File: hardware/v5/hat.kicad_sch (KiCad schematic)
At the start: 6 parts, among them J1 GPIO, U1 CAT24C256

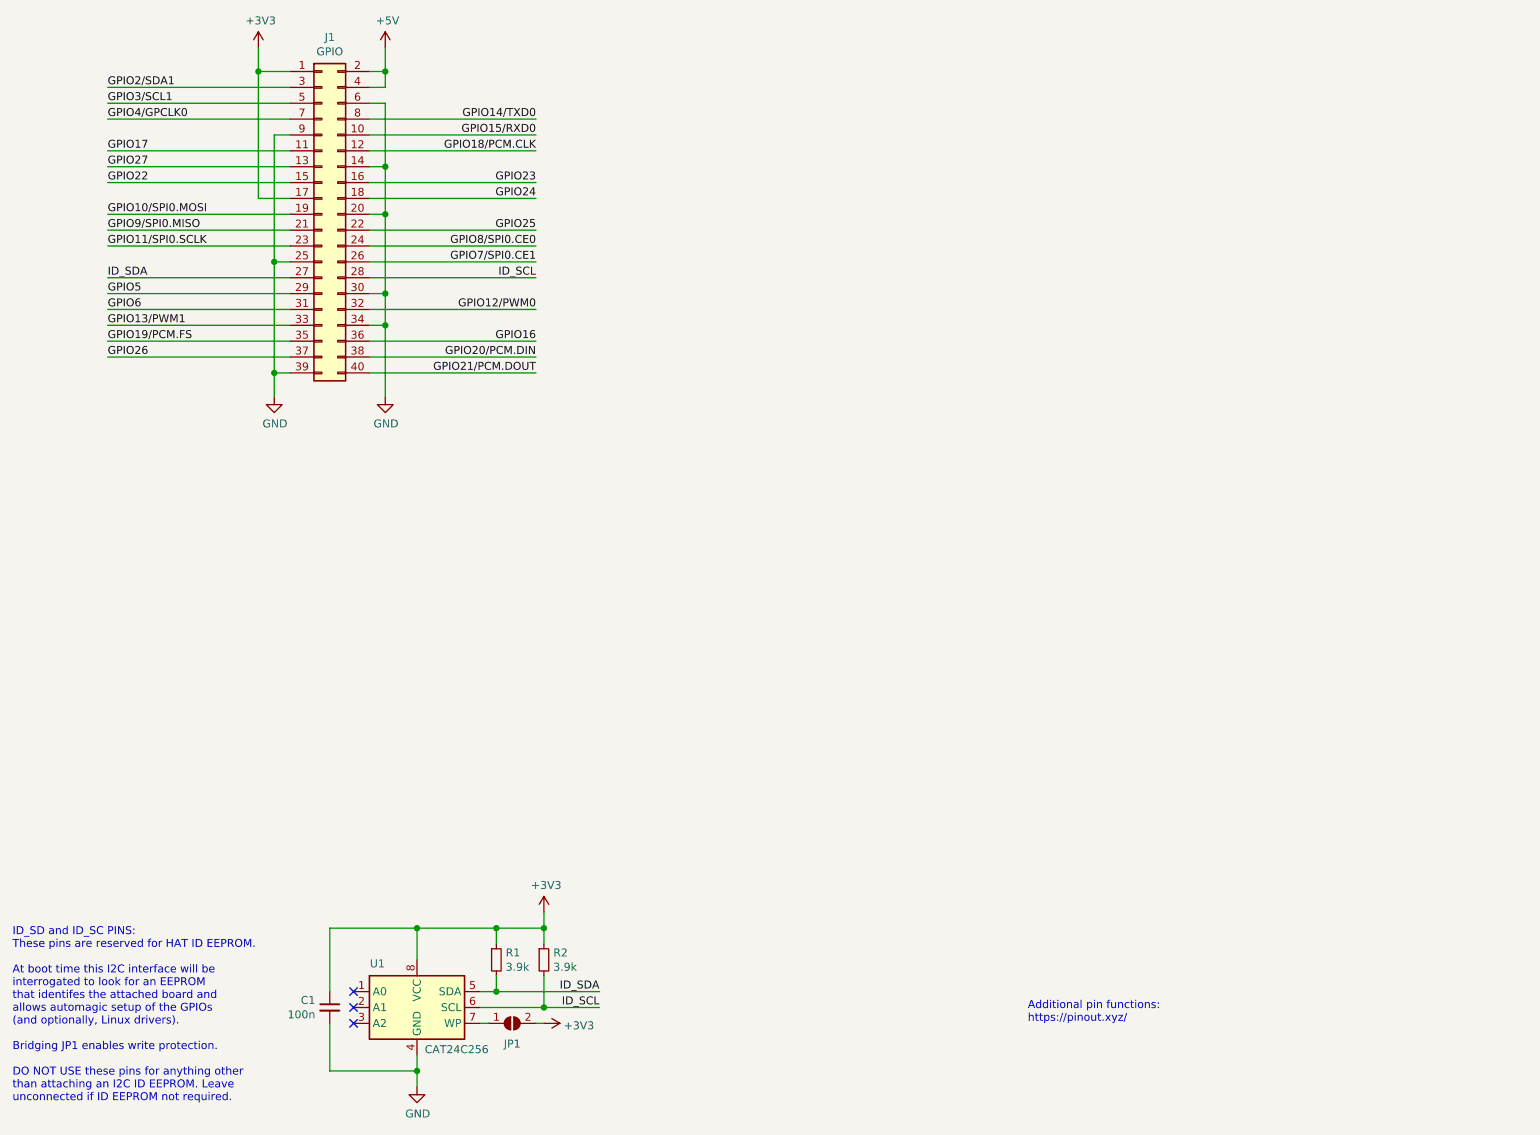
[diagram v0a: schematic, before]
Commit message: v5: import/reimplement parport design on template
Problem: template board is still blank.

Adjust board edge to handle SMT header and add cutout for pi5 camera/
display FFC connectors.  For GPIO connector, use existing kicad 8 Harwin
M20 series footprint but adjust the pinout for top of board pi GPIO,
and adjust position since centroid moved from THT pin 1 to SMT centroid.
Add keepout for pi5 PoE like the existing one for pi4.

Import the SN74LVC16128 symbol from the v4 board.  Orient the chip
as before for best routing but aim for tighter traces this time.
Add bypass caps to all power inputs for good measure.  Chip capacitors
and resistors are shrunk from 0805 to 0603 in this revision.  Allow the
cable VCC to be jumpered to either 5V or 3V3 per the spec sheet.

Move the EEPROM to the east end of the board for more direct routing.
Add a strong 1K pull-up to the template's WP jumper per the HAT+ spec.
Orient the chip the same direction as the SN74LVC16128 to avoid confusion.

Add the DB-25 right-angle 2x13 header on the west end as before.
This time, use a custom header footprint so the DB-25 pin numbers can
be mirrored on the header.  Also, add a board cutout to improve insertion
ergonmics if the right angle header is used.

Implement the GPIO reassignments proposed in #67.  This should allow
I2C, UART0, and PWM0 to be used in stacked HATs.

Add a Sparkfun Qwiic connector to allow I2C expansion that way as well.
See: https://www.sparkfun.com/qwiic.

Put the official HAT+ logo on the board since this board complies with
https://datasheets.raspberrypi.com/hat/hat-plus-specification.pdf.
The logo image was provided via email along with marking guidelines.
Use the minimum 2.25mm height specified in the guidelines.

Add some helpful notes and the DB-25 pinout to the board silkscreen.
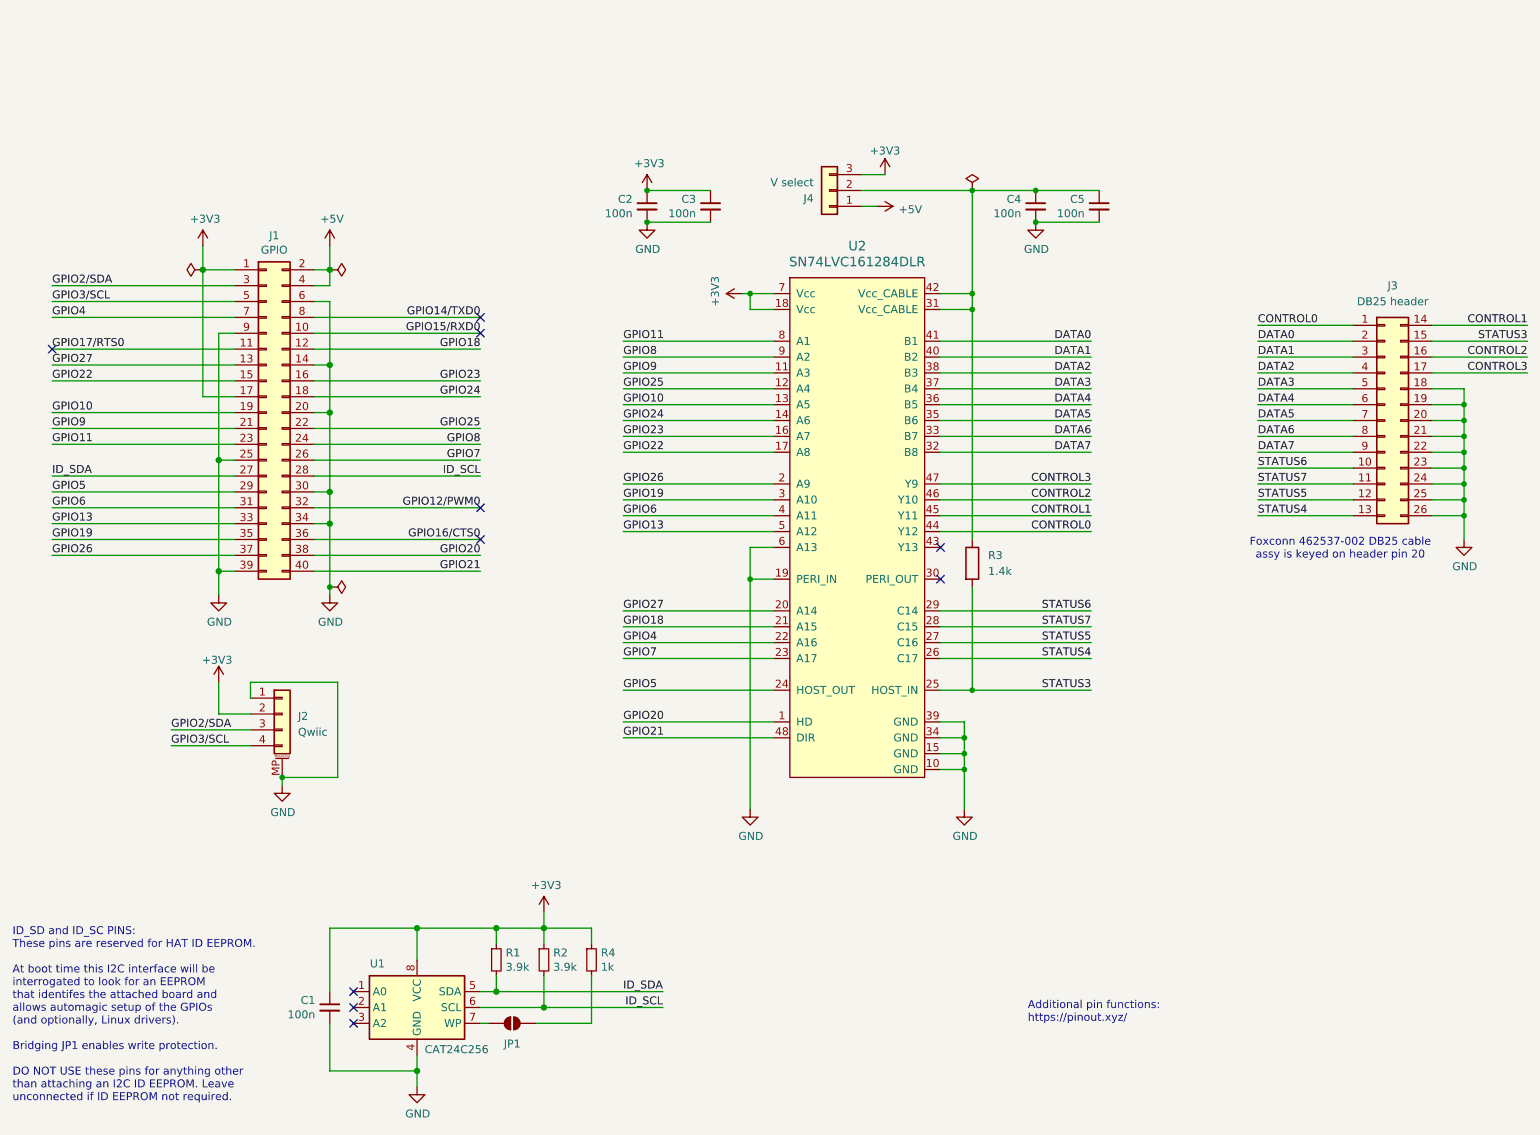
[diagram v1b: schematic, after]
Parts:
- added C2, C3, C4, C5: 100n, Capacitor_SMD:C_0603_1608Metric, symbol Device:C_Small
- added J2: Qwiic, Connector_JST:JST_SH_SM04B-SRSS-TB_1x04-1MP_P1.00mm_Horizontal, symbol Connector_Generic_MountingPin:Conn_01x04_MountingPin
- added J3: DB25 header, lib:DB25_header_2x13_P2.54mm_horizontal, symbol Connector_Generic:Conn_02x13_Top_Bottom
- added J4: V select, Connector_PinHeader_2.54mm:PinHeader_1x03_P2.54mm_Vertical, symbol Connector_Generic:Conn_01x03
- added R3: 1.4k, Resistor_SMD:R_0603_1608Metric, symbol Device:R
- added R4: 1k, Resistor_SMD:R_0603_1608Metric, symbol Device:R_Small
- added U2: SN74LVC161284DLR, Package_SO:SSOP-48_7.5x15.9mm_P0.635mm, symbol SN74LVC16128:SN74LVC161284DLR
- C1: footprint (none) -> Capacitor_SMD:C_0603_1608Metric
- J1: footprint Connector_PinSocket_2.54mm:PinSocket_2x20_P2.54mm_Vertical -> lib:Harwin_M20-7812045_2x20_P2.54mm_Vertical
- JP1: footprint (none) -> Jumper:SolderJumper-2_P1.3mm_Open_RoundedPad1.0x1.5mm
- R1, R2: footprint (none) -> Resistor_SMD:R_0603_1608Metric
- U1: footprint (none) -> Package_SO:SOIC-8_3.9x4.9mm_P1.27mm
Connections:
- net +3V3: now also C2.1, C3.1, J2.2 (Pin_2), J4.3 (Pin_3), R4.1, U2.18 (Vcc), U2.7 (Vcc); no longer JP1.2 (B)
- net +5V: now also J4.1 (Pin_1)
- net GND: now also C2.2, C3.2, C4.2, C5.2, J2.1 (Pin_1), J2.MP (MountPin), J3.18 (Pin_18), J3.19 (Pin_19), J3.20 (Pin_20), J3.21 (Pin_21), J3.22 (Pin_22), J3.23 (Pin_23), J3.24 (Pin_24), J3.25 (Pin_25), J3.26 (Pin_26), U2.10 (GND), U2.15 (GND), U2.19 (PERI_IN), U2.34 (GND), U2.39 (GND), U2.6 (A13)
- net GPIO22: now also U2.17 (A8)
- net GPIO23: now also U2.16 (A7)
- net GPIO24: now also U2.14 (A6)
- net GPIO25: now also U2.12 (A4)
- net GPIO26: now also U2.2 (A9)
- net GPIO27: now also U2.20 (A14)
- net GPIO5: now also U2.24 (HOST_OUT)
- net GPIO6: now also U2.4 (A11)
- net GPIO10/SPI0.MOSI renamed GPIO10
- net GPIO10: now also U2.13 (A5)
- net GPIO11/SPI0.SCLK renamed GPIO11
- net GPIO11: now also U2.8 (A1)
- net GPIO13/PWM1 renamed GPIO13
- net GPIO13: now also U2.5 (A12)
- net GPIO16 renamed GPIO16/CTS0
- net GPIO17 renamed GPIO17/RTS0
- net GPIO18/PCM.CLK renamed GPIO18
- net GPIO18: now also U2.21 (A15)
- net GPIO19/PCM.FS renamed GPIO19
- net GPIO19: now also U2.3 (A10)
- net GPIO20/PCM.DIN renamed GPIO20
- net GPIO20: now also U2.1 (HD)
- net GPIO21/PCM.DOUT renamed GPIO21
- net GPIO21: now also U2.48 (DIR)
- net GPIO2/SDA1 renamed GPIO2/SDA
- net GPIO2/SDA: now also J2.3 (Pin_3)
- net GPIO3/SCL1 renamed GPIO3/SCL
- net GPIO3/SCL: now also J2.4 (Pin_4)
- net GPIO4/GPCLK0 renamed GPIO4
- net GPIO4: now also U2.22 (A16)
- net GPIO7/SPI0.CE1 renamed GPIO7
- net GPIO7: now also U2.23 (A17)
- net GPIO8/SPI0.CE0 renamed GPIO8
- net GPIO8: now also U2.9 (A2)
- net GPIO9/SPI0.MISO renamed GPIO9
- net GPIO9: now also U2.11 (A3)
- new net: C4.1, C5.1, J4.2 (Pin_2), R3.1, U2.31 (Vcc_CABLE), U2.42 (Vcc_CABLE)
- new net: JP1.2 (B), R4.2
- new net CONTROL0: J3.1 (Pin_1), U2.44 (Y12)
- new net CONTROL1: J3.14 (Pin_14), U2.45 (Y11)
- new net CONTROL2: J3.16 (Pin_16), U2.46 (Y10)
- new net CONTROL3: J3.17 (Pin_17), U2.47 (Y9)
- new net DATA0: J3.2 (Pin_2), U2.41 (B1)
- new net DATA1: J3.3 (Pin_3), U2.40 (B2)
- new net DATA2: J3.4 (Pin_4), U2.38 (B3)
- new net DATA3: J3.5 (Pin_5), U2.37 (B4)
- new net DATA4: J3.6 (Pin_6), U2.36 (B5)
- new net DATA5: J3.7 (Pin_7), U2.35 (B6)
- new net DATA6: J3.8 (Pin_8), U2.33 (B7)
- new net DATA7: J3.9 (Pin_9), U2.32 (B8)
- new net STATUS3: J3.15 (Pin_15), R3.2, U2.25 (HOST_IN)
- new net STATUS4: J3.13 (Pin_13), U2.26 (C17)
- new net STATUS5: J3.12 (Pin_12), U2.27 (C16)
- new net STATUS6: J3.10 (Pin_10), U2.29 (C14)
- new net STATUS7: J3.11 (Pin_11), U2.28 (C15)
- no-connect marks 3 -> 10
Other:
- note added: "Foxconn 462537-002 DB25 cable assy is keyed on header pin 20"
- title: Pi Parallel Port HAT+ -> IEEE Std 1284 HAT+
- moved on the sheet: J1

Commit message: v5: add BOM data needed for JLCPCB assembly
Problem: component metadata is not in a form that could be sent
out for assembly.

Add BOM fields recommended for JLCPCB assembly[1] and fill in.

[1] https://jlcpcb.com/help/article/How-to-generate-the-BOM-and-Centroid-file-from-KiCAD
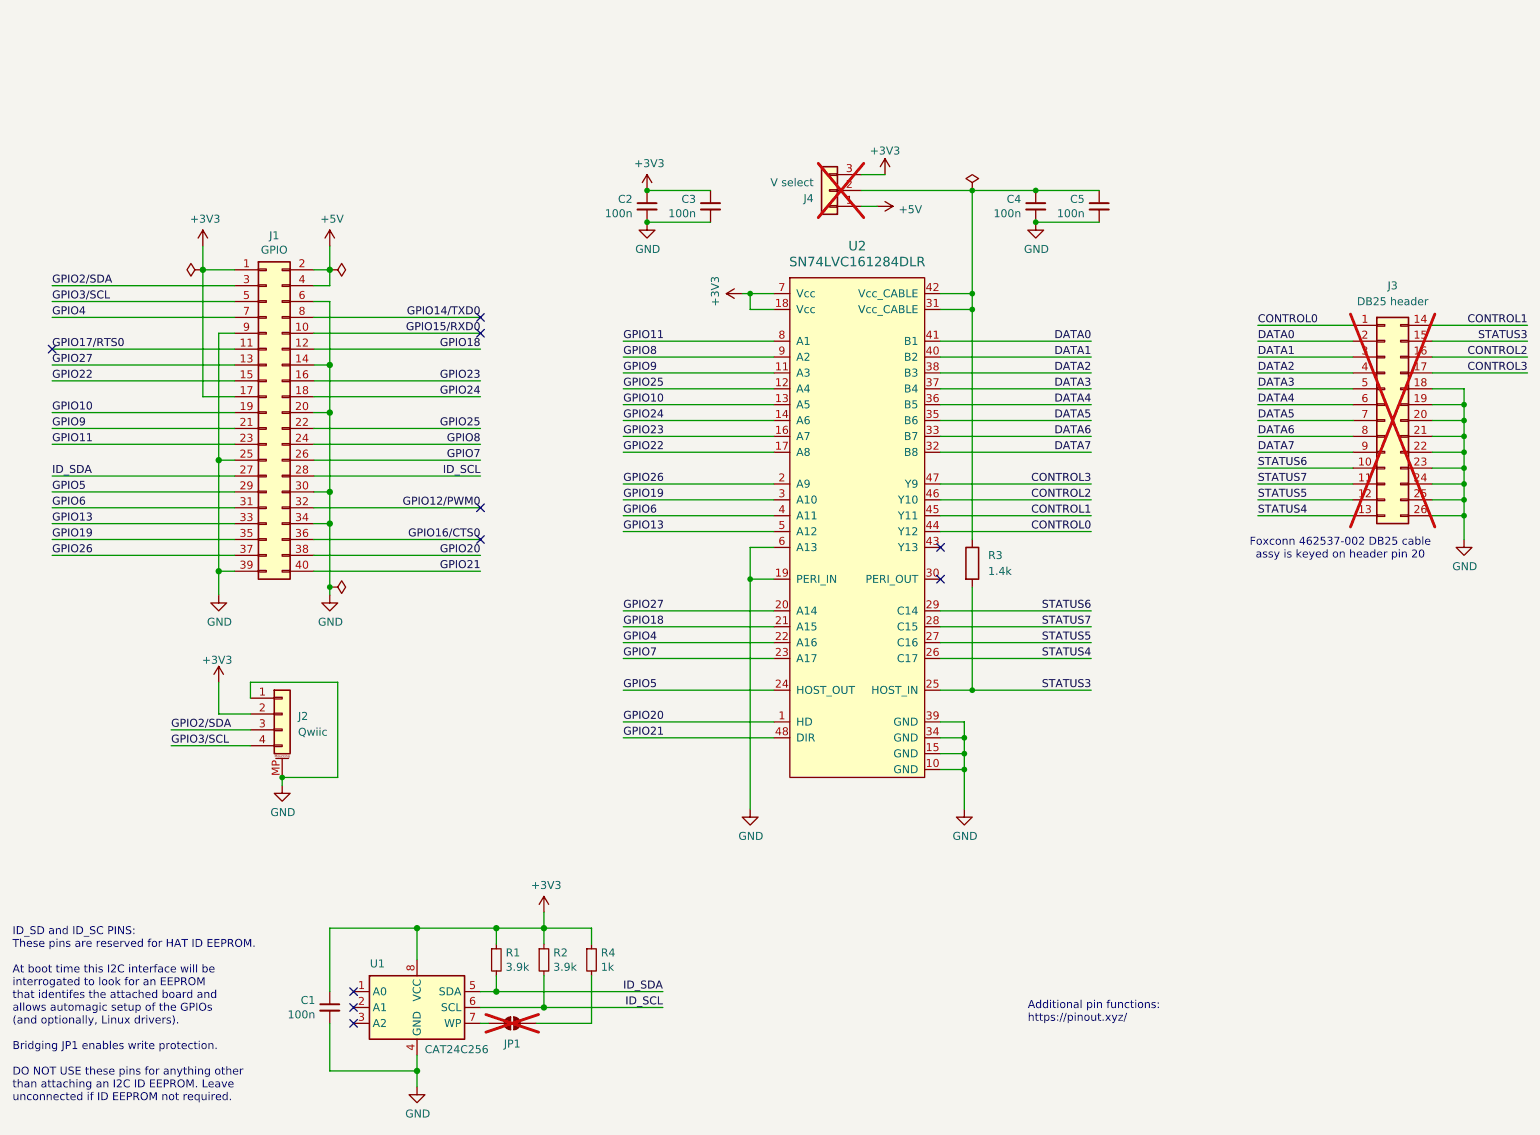
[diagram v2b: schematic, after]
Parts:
- C1, C2, C3, C4, C5: Comment (none) -> 100nF 25V MLCC; LCSC (none) -> C346189
- J1: Comment (none) -> Harwin M20-7812045 or equiv; Mouser (none) -> 855-M20-7812045
- J2: Comment (none) -> JST SM04-SRSS-TB; Mouser (none) -> 306-SM04BSRSSTBLFSNP
- J3, J4, JP1: now not fitted
- R1, R2: Comment (none) -> 3K9 100mW 1%; LCSC (none) -> C144659
- R3: Comment (none) -> 1K4 100mW 1%; LCSC (none) -> C705740
- R4: Comment (none) -> 1K 100mW 1%; LCSC (none) -> C110776
- U1: Comment (none) -> CAT24C256WI-GT3; LCSC (none) -> C79987
- U2: Comment (none) -> SN74LVC161284DLR; Digi-Key_PN 296-8467-5-ND -> (none); MPN SN74LVC161284DL -> (none); Manufacturer Texas Instruments -> (none); Mouser (none) -> 595-SN74LVC161284DLR; Package 48-SSOP -> (none)

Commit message: v5: update BOM with LCSC parts
Problem: JLC PCBA is faster/cheaper if parts can be sourced
from LCSC in China.

Based on input from a JLC engineer, update the BOM with LCSC parts.
U2 is unavailable and will have to be ordered by them from Mouser.

Note the Harwin M20-7812045 2x20 SMT header is $3.31 ea in Qty 11
(Mouser), but the equivalent Liansheng FH-00339 is $0.40 ea in Qty 10.

Update BOM.
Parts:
- J1: Comment Harwin M20-7812045 or equiv -> SMT 2x20 2.54mm vert female header top/bottom entry, h<=4mm; LCSC (none) -> C2685112
- J2: LCSC (none) -> C2845363
- R1, R2: LCSC C144659 -> C114616
- R3: LCSC C705740 -> C185359
- R4: LCSC C110776 -> C21190
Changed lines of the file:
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@@
 			)
 		)
-		(property "Comment" "Harwin M20-7812045 or equiv"
+		(property "Comment" "SMT 2x20 2.54mm vert female header top/bottom entry, h<=4mm"
 			(at 57.15 82.55 0)
 			(effects
@@
 			)
 		)
-		(property "LCSC" ""
+		(property "LCSC" "C2685112"
 			(at 57.15 82.55 0)
 			(effects
@@
 			)
 		)
-		(property "LCSC" "C144659"
+		(property "LCSC" "C114616"
 			(at 93.98 170.18 0)
 			(effects
@@
 			)
 		)
-		(property "LCSC" "C705740"
+		(property "LCSC" "C185359"
 			(at 170.18 106.68 0)
 			(effects
@@
 			)
 		)
-		(property "LCSC" "C144659"
+		(property "LCSC" "C114616"
 			(at 101.6 170.18 0)
 			(effects
@@
 			)
 		)
-		(property "LCSC" ""
+		(property "LCSC" "C2845363"
 			(at 59.69 130.81 0)
 			(effects
@@
 			)
 		)
-		(property "LCSC" "C110776"
+		(property "LCSC" "C21190"
 			(at 109.22 170.18 0)
 			(effects

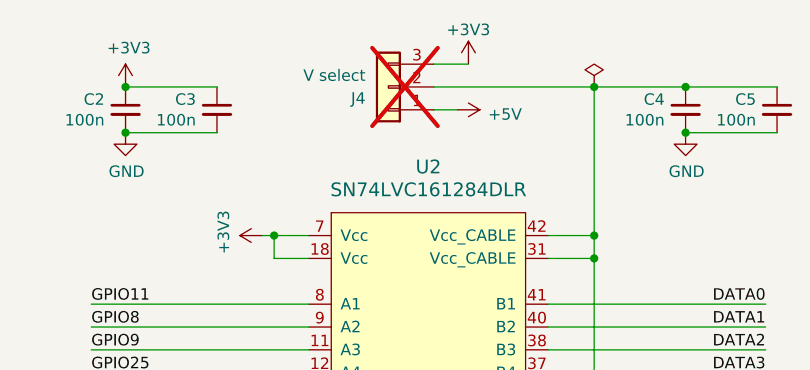
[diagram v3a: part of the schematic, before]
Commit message: v5: switch J4 to SMT
Problem: the J4 1x3 header is a through hole part that is marked
"do not place" so it can be installed by hand.

Switch J4 to an SMT footprint and uncheck DNP.
Adjust board routing.
Add a LCSC part number to the BOM.
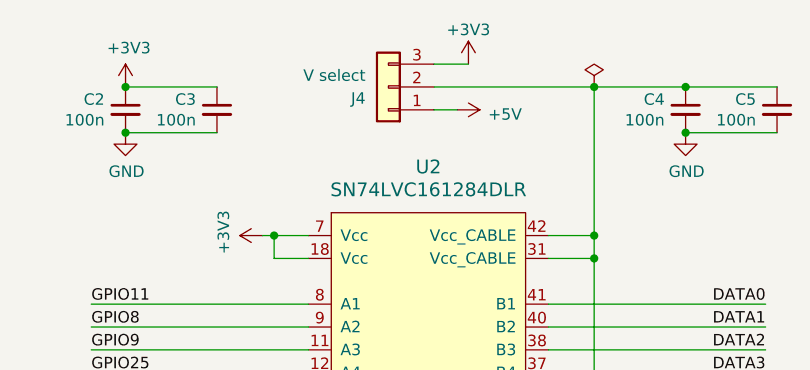
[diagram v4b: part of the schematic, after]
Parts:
- J4: footprint Connector_PinHeader_2.54mm:PinHeader_1x03_P2.54mm_Vertical -> Connector_PinHeader_2.54mm:PinHeader_1x03_P2.54mm_Vertical_SMD_Pin1Left; Comment (none) -> SMT 1x3 2.54mm pin header; LCSC (none) -> C2883760; now fitted
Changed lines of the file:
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@@
 		(in_bom yes)
 		(on_board yes)
-		(dnp yes)
+		(dnp no)
 		(fields_autoplaced yes)
 		(property "Reference" "J4"
@@
 			)
 		)
-		(property "Footprint" "Connector_PinHeader_2.54mm:PinHeader_1x03_P2.54mm_Vertical"
+		(property "Footprint" "Connector_PinHeader_2.54mm:PinHeader_1x03_P2.54mm_Vertical_SMD_Pin1Left"
 			(at 147.32 46.99 0)
 			(effects
@@
 			)
 		)
-		(property "Comment" ""
+		(property "Comment" "SMT 1x3 2.54mm pin header"
 			(at 147.32 46.99 0)
 			(effects
@@
 			)
 		)
-		(property "LCSC" ""
+		(property "LCSC" "C2883760"
 			(at 147.32 46.99 0)
 			(effects
